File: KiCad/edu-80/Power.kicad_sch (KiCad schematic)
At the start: 5 parts, among them U11 CD4093, U12 4027, U13 4001, U16 7400

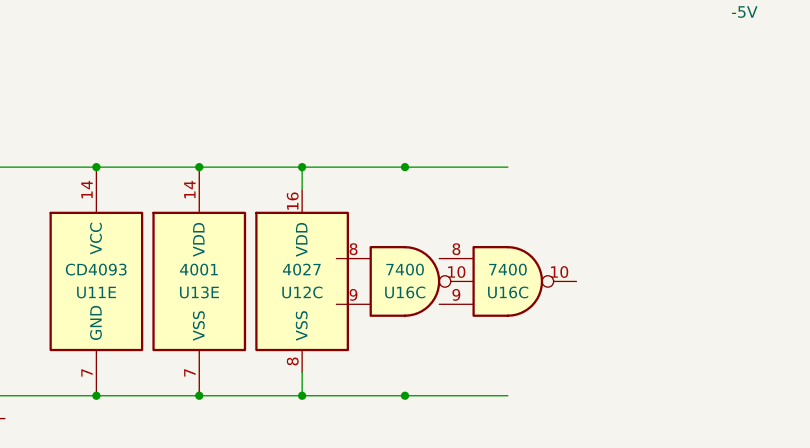
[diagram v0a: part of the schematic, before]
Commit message: Fixed lst of the errors, still two warnings
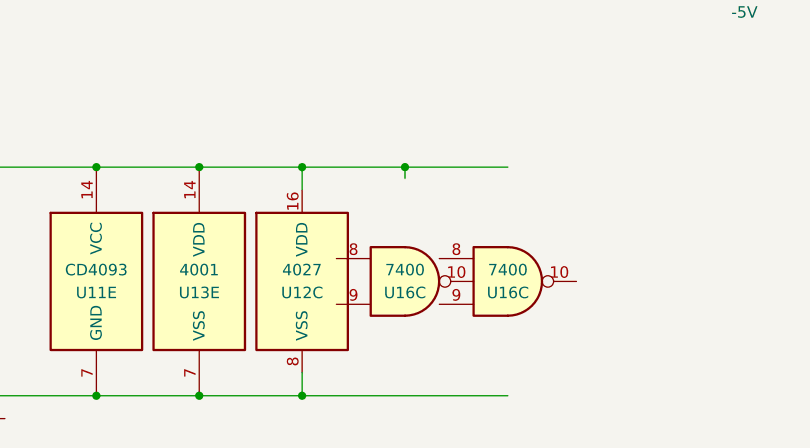
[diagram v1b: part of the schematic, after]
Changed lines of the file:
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@@
 (kicad_sch (version 20230121) (generator eeschema)
   (paper "A")
-  (junction (at 76.2 92.71) (diameter 0) (color 0 0 0 0)
-  )
   (junction (at 41.91 92.71) (diameter 0) (color 0 0 0 0)
   )
@@
   )
   (junction (at 53.34 92.71) (diameter 0) (color 0 0 0 0)
-  )
-  (junction (at 76.2 118.11) (diameter 0) (color 0 0 0 0)
   )
   (junction (at 114.3 68.58) (diameter 0) (color 0 0 0 0)
@@
   )
   (junction (at 88.9 52.07) (diameter 0) (color 0 0 0 0)
+  )
+  (junction (at 76.2 92.71) (diameter 0) (color 0 0 0 0)
   )
   (junction (at 139.7 68.58) (diameter 0) (color 0 0 0 0)
@@
     (stroke (width 0) (type default))
   )
-  (wire (pts (xy 76.2 92.71) (xy 87.63 92.71))
-    (stroke (width 0) (type default))
-  )
   (wire (pts (xy 64.77 92.71) (xy 76.2 92.71))
     (stroke (width 0) (type default))
@@
     (stroke (width 0) (type default))
   )
+  (wire (pts (xy 64.77 118.11) (xy 87.63 118.11))
+    (stroke (width 0) (type default))
+  )
   (wire (pts (xy 139.7 68.58) (xy 139.7 63.5))
     (stroke (width 0) (type default))
@@
     (stroke (width 0) (type default))
   )
-  (wire (pts (xy 63.5 31.75) (xy 63.5 38.1))
+  (wire (pts (xy 114.3 71.12) (xy 114.3 68.58))
     (stroke (width 0) (type default))
   )
-  (wire (pts (xy 64.77 118.11) (xy 76.2 118.11))
-    (stroke (width 0) (type default))
-  )
-  (wire (pts (xy 114.3 71.12) (xy 114.3 68.58))
+  (wire (pts (xy 63.5 31.75) (xy 63.5 38.1))
     (stroke (width 0) (type default))
   )
@@
     (stroke (width 0) (type default))
   )
-  (wire (pts (xy 76.2 118.11) (xy 87.63 118.11))
+  (wire (pts (xy 76.2 92.71) (xy 76.2 93.98))
     (stroke (width 0) (type default))
   )
@@
     (stroke (width 0) (type default))
   )
+  (wire (pts (xy 76.2 92.71) (xy 87.63 92.71))
+    (stroke (width 0) (type default))
+  )

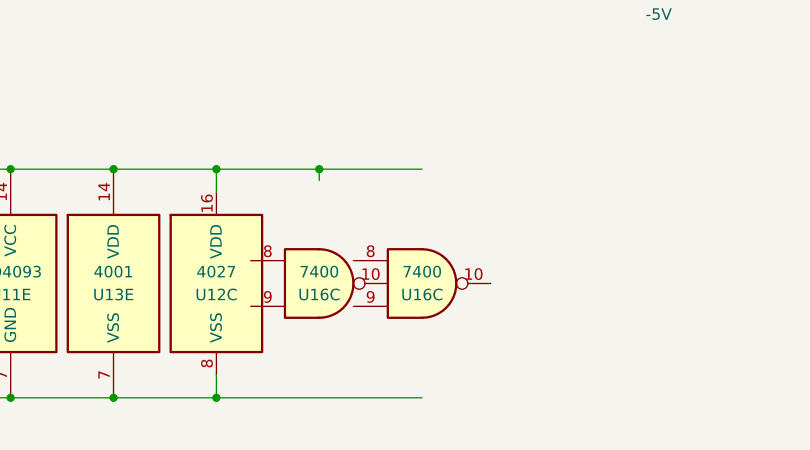
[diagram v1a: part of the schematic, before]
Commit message: Working on removing edu-80-rescue symbol library
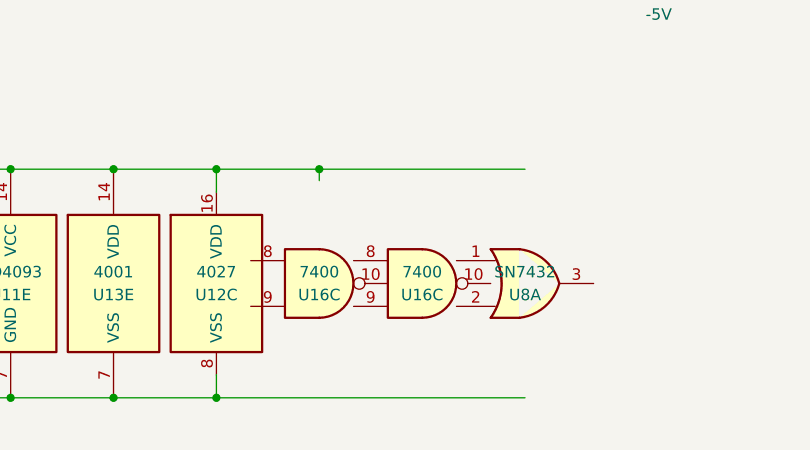
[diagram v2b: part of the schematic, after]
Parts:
- added U8: SN7432, symbol Edu-80_Symbols:SN7432
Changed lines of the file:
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@@
 (kicad_sch (version 20230121) (generator eeschema)
   (paper "A")
+  (junction (at 64.77 118.11) (diameter 0) (color 0 0 0 0)
+  )
   (junction (at 41.91 92.71) (diameter 0) (color 0 0 0 0)
   )
   (junction (at 38.1 34.29) (diameter 0) (color 0 0 0 0)
   )
-  (junction (at 64.77 118.11) (diameter 0) (color 0 0 0 0)
-  )
   (junction (at 53.34 92.71) (diameter 0) (color 0 0 0 0)
   )
@@
     (stroke (width 0) (type default))
   )
+  (wire (pts (xy 76.2 92.71) (xy 99.06 92.71))
+    (stroke (width 0) (type default))
+  )
   (wire (pts (xy 38.1 31.75) (xy 38.1 34.29))
     (stroke (width 0) (type default))
@@
     (stroke (width 0) (type default))
   )
-  (wire (pts (xy 64.77 118.11) (xy 87.63 118.11))
-    (stroke (width 0) (type default))
-  )
   (wire (pts (xy 139.7 68.58) (xy 139.7 63.5))
     (stroke (width 0) (type default))
@@
     (stroke (width 0) (type default))
   )
-  (wire (pts (xy 76.2 92.71) (xy 87.63 92.71))
+  (wire (pts (xy 64.77 118.11) (xy 99.06 118.11))
     (stroke (width 0) (type default))
   )
@@
         )
       )
+    )
+  )
+  (symbol (lib_id "Edu-80_Symbols:SN7432") (at 99.06 105.41 0) (unit 1)
+    (in_bom yes) (on_board yes) (dnp no)
+    (property "Reference" "U8" (at 99.06 106.68 0)
+      (effects (font (size 1.27 1.27)))
+    )
+    (property "Value" "SN7432" (at 99.06 104.14 0)
+      (effects (font (size 1.27 1.27)))
+    )
+    (property "Footprint" "" (at 99.06 105.41 0)
+      (effects (font (size 1.27 1.27)) hide)
+    )
+    (property "Datasheet" "" (at 99.06 105.41 0)
+      (effects (font (size 1.27 1.27)) hide)
+    )
+    (pin "1")
+    (pin "2")
+    (pin "3")
+    (pin "4")
+    (pin "5")
+    (pin "6")
+    (pin "10")
+    (pin "8")
+    (pin "9")
+    (pin "11")
+    (pin "12")
+    (pin "13")
+    (pin "14")
+    (pin "7")
+    (instances
+      (project "edu-80"
+        (path "/d19d6db6-a96a-43e3-aa50-c057821f7e22/00000000-0000-0000-0000-000063e35f90"
+          (reference "U8") (unit 1)
+        )
+        (path "/d19d6db6-a96a-43e3-aa50-c057821f7e22/00000000-0000-0000-0000-0000644ab222"
+          (reference "U8") (unit 5)
+        )
+      )

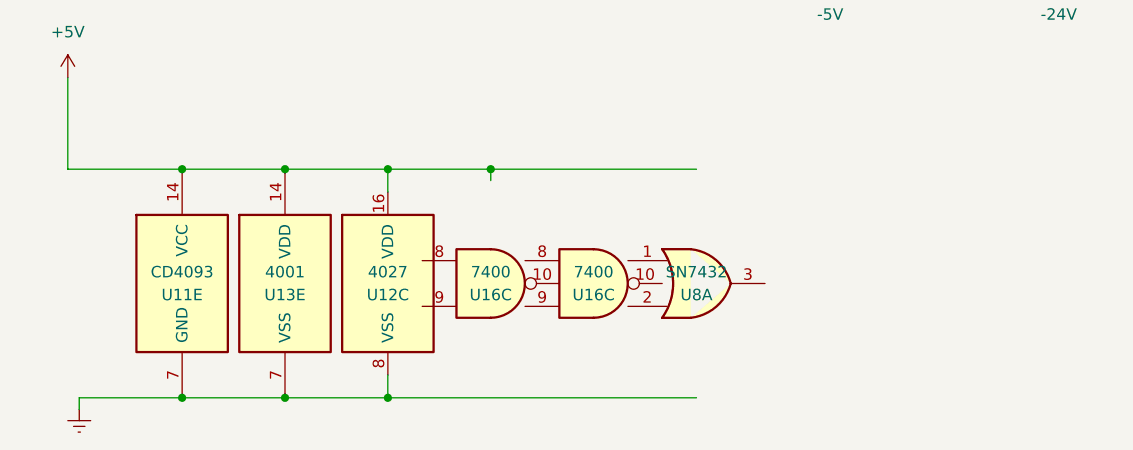
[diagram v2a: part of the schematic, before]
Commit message: Cleaning up the PAL-003 decoding, adding Modifications page.
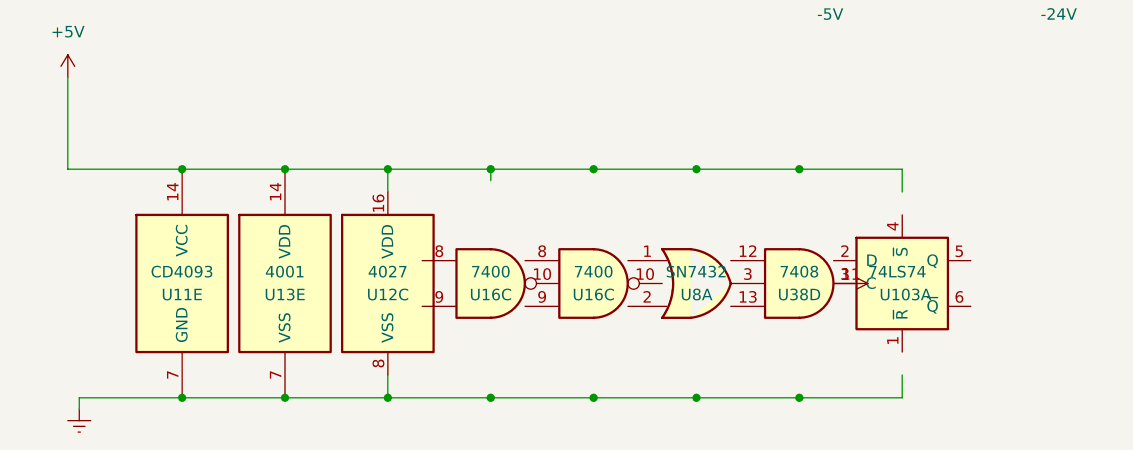
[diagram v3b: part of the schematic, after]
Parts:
- added U103: 74LS74, symbol 74xx:74LS74
- added U38: 7408, symbol Edu-80_Symbols:7408
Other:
- company: (none) -> Strangers
- title: (none) -> Edu-80 Z80 Trainer
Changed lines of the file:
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@@
 (kicad_sch (version 20230121) (generator eeschema)
   (paper "A")
+  (title_block
+    (title "Edu-80 Z80 Trainer")
+    (date "2023-06-03")
+    (rev "0.1")
+    (company "Strangers")
+    (comment 1 "Author: James D. Tucker")
+  )
+  (junction (at 38.1 34.29) (diameter 0) (color 0 0 0 0)
+  )
+  (junction (at 53.34 118.11) (diameter 0) (color 0 0 0 0)
+  )
+  (junction (at 87.63 118.11) (diameter 0) (color 0 0 0 0)
+  )
+  (junction (at 41.91 92.71) (diameter 0) (color 0 0 0 0)
+  )
+  (junction (at 114.3 68.58) (diameter 0) (color 0 0 0 0)
+  )
+  (junction (at 76.2 92.71) (diameter 0) (color 0 0 0 0)
+  )
+  (junction (at 53.34 92.71) (diameter 0) (color 0 0 0 0)
+  )
+  (junction (at 99.06 118.11) (diameter 0) (color 0 0 0 0)
+  )
+  (junction (at 64.77 92.71) (diameter 0) (color 0 0 0 0)
+  )
+  (junction (at 87.63 92.71) (diameter 0) (color 0 0 0 0)
+  )
+  (junction (at 110.49 92.71) (diameter 0) (color 0 0 0 0)
+  )
+  (junction (at 41.91 118.11) (diameter 0) (color 0 0 0 0)
+  )
+  (junction (at 110.49 118.11) (diameter 0) (color 0 0 0 0)
+  )
+  (junction (at 88.9 52.07) (diameter 0) (color 0 0 0 0)
+  )
+  (junction (at 139.7 68.58) (diameter 0) (color 0 0 0 0)
+  )
+  (junction (at 76.2 118.11) (diameter 0) (color 0 0 0 0)
+  )
+  (junction (at 99.06 92.71) (diameter 0) (color 0 0 0 0)
+  )
   (junction (at 64.77 118.11) (diameter 0) (color 0 0 0 0)
   )
-  (junction (at 41.91 92.71) (diameter 0) (color 0 0 0 0)
-  )
-  (junction (at 38.1 34.29) (diameter 0) (color 0 0 0 0)
-  )
-  (junction (at 53.34 92.71) (diameter 0) (color 0 0 0 0)
-  )
-  (junction (at 114.3 68.58) (diameter 0) (color 0 0 0 0)
-  )
-  (junction (at 64.77 92.71) (diameter 0) (color 0 0 0 0)
-  )
-  (junction (at 41.91 118.11) (diameter 0) (color 0 0 0 0)
-  )
-  (junction (at 53.34 118.11) (diameter 0) (color 0 0 0 0)
-  )
-  (junction (at 88.9 52.07) (diameter 0) (color 0 0 0 0)
-  )
-  (junction (at 76.2 92.71) (diameter 0) (color 0 0 0 0)
-  )
-  (junction (at 139.7 68.58) (diameter 0) (color 0 0 0 0)
+  (wire (pts (xy 99.06 118.11) (xy 110.49 118.11))
+    (stroke (width 0) (type default))
+  )
+  (wire (pts (xy 121.92 92.71) (xy 110.49 92.71))
+    (stroke (width 0) (type default))
+  )
+  (wire (pts (xy 41.91 92.71) (xy 53.34 92.71))
+    (stroke (width 0) (type default))
   )
   (wire (pts (xy 64.77 115.57) (xy 64.77 118.11))
     (stroke (width 0) (type default))
   )
-  (wire (pts (xy 41.91 92.71) (xy 53.34 92.71))
+  (wire (pts (xy 30.48 118.11) (xy 41.91 118.11))
+    (stroke (width 0) (type default))
+  )
+  (wire (pts (xy 41.91 118.11) (xy 53.34 118.11))
     (stroke (width 0) (type default))
   )
@@
     (stroke (width 0) (type default))
   )
+  (wire (pts (xy 87.63 92.71) (xy 99.06 92.71))
+    (stroke (width 0) (type default))
+  )
   (wire (pts (xy 139.7 71.12) (xy 139.7 68.58))
     (stroke (width 0) (type default))
   )
+  (wire (pts (xy 64.77 118.11) (xy 76.2 118.11))
+    (stroke (width 0) (type default))
+  )
+  (wire (pts (xy 29.21 92.71) (xy 41.91 92.71))
+    (stroke (width 0) (type default))
+  )
+  (wire (pts (xy 38.1 31.75) (xy 38.1 34.29))
+    (stroke (width 0) (type default))
+  )
+  (wire (pts (xy 194.31 39.37) (xy 194.31 46.99))
+    (stroke (width 0) (type default))
+  )
+  (wire (pts (xy 139.7 68.58) (xy 139.7 63.5))
+    (stroke (width 0) (type default))
+  )
+  (wire (pts (xy 121.92 115.57) (xy 121.92 118.11))
+    (stroke (width 0) (type default))
+  )
+  (wire (pts (xy 76.2 92.71) (xy 87.63 92.71))
+    (stroke (width 0) (type default))
+  )
+  (wire (pts (xy 99.06 92.71) (xy 110.49 92.71))
+    (stroke (width 0) (type default))
+  )
+  (wire (pts (xy 114.3 71.12) (xy 114.3 68.58))
+    (stroke (width 0) (type default))
+  )
+  (wire (pts (xy 63.5 31.75) (xy 63.5 38.1))
+    (stroke (width 0) (type default))
+  )
+  (wire (pts (xy 29.21 92.71) (xy 29.21 82.55))
+    (stroke (width 0) (type default))
+  )
+  (wire (pts (xy 88.9 52.07) (xy 88.9 46.99))
+    (stroke (width 0) (type default))
+  )
+  (wire (pts (xy 76.2 92.71) (xy 76.2 93.98))
+    (stroke (width 0) (type default))
+  )
+  (wire (pts (xy 121.92 95.25) (xy 121.92 92.71))
+    (stroke (width 0) (type default))
+  )
+  (wire (pts (xy 53.34 118.11) (xy 64.77 118.11))
+    (stroke (width 0) (type default))
+  )
+  (wire (pts (xy 53.34 92.71) (xy 64.77 92.71))
+    (stroke (width 0) (type default))
+  )
+  (wire (pts (xy 168.91 39.37) (xy 168.91 46.99))
+    (stroke (width 0) (type default))
+  )
+  (wire (pts (xy 64.77 92.71) (xy 64.77 95.25))
+    (stroke (width 0) (type default))
+  )
+  (wire (pts (xy 121.92 118.11) (xy 110.49 118.11))
+    (stroke (width 0) (type default))
+  )
+  (wire (pts (xy 114.3 68.58) (xy 114.3 63.5))
+    (stroke (width 0) (type default))
+  )
+  (wire (pts (xy 87.63 118.11) (xy 99.06 118.11))
+    (stroke (width 0) (type default))
+  )
   (wire (pts (xy 64.77 92.71) (xy 76.2 92.71))
     (stroke (width 0) (type default))
   )
-  (wire (pts (xy 41.91 118.11) (xy 53.34 118.11))
-    (stroke (width 0) (type default))
-  )
-  (wire (pts (xy 76.2 92.71) (xy 99.06 92.71))
-    (stroke (width 0) (type default))
-  )
-  (wire (pts (xy 38.1 31.75) (xy 38.1 34.29))
-    (stroke (width 0) (type default))
-  )
-  (wire (pts (xy 194.31 39.37) (xy 194.31 46.99))
-    (stroke (width 0) (type default))
-  )
-  (wire (pts (xy 139.7 68.58) (xy 139.7 63.5))
-    (stroke (width 0) (type default))
-  )
-  (wire (pts (xy 64.77 118.11) (xy 53.34 118.11))
-    (stroke (width 0) (type default))
-  )
-  (wire (pts (xy 114.3 71.12) (xy 114.3 68.58))
-    (stroke (width 0) (type default))
-  )
-  (wire (pts (xy 63.5 31.75) (xy 63.5 38.1))
-    (stroke (width 0) (type default))
-  )
-  (wire (pts (xy 41.91 118.11) (xy 30.48 118.11))
-    (stroke (width 0) (type default))
-  )
-  (wire (pts (xy 29.21 92.71) (xy 41.91 92.71))
-    (stroke (width 0) (type default))
-  )
-  (wire (pts (xy 29.21 92.71) (xy 29.21 82.55))
-    (stroke (width 0) (type default))
-  )
-  (wire (pts (xy 88.9 52.07) (xy 88.9 46.99))
-    (stroke (width 0) (type default))
-  )
-  (wire (pts (xy 76.2 92.71) (xy 76.2 93.98))
-    (stroke (width 0) (type default))
-  )
-  (wire (pts (xy 168.91 39.37) (xy 168.91 46.99))
-    (stroke (width 0) (type default))
-  )
-  (wire (pts (xy 64.77 118.11) (xy 99.06 118.11))
-    (stroke (width 0) (type default))
-  )
-  (wire (pts (xy 53.34 92.71) (xy 64.77 92.71))
-    (stroke (width 0) (type default))
-  )
-  (wire (pts (xy 64.77 92.71) (xy 64.77 95.25))
-    (stroke (width 0) (type default))
-  )
-  (wire (pts (xy 114.3 68.58) (xy 114.3 63.5))
+  (wire (pts (xy 76.2 118.11) (xy 87.63 118.11))
     (stroke (width 0) (type default))
   )
@@
     )
   )
+  (symbol (lib_id "74xx:74LS74") (at 121.92 105.41 0) (unit 1)
+    (in_bom yes) (on_board yes) (dnp no)
+    (property "Reference" "U103" (at 119.38 106.68 0)
+      (effects (font (size 1.27 1.27)) (justify left))
+    )
+    (property "Value" "74LS74" (at 118.11 104.14 0)
+      (effects (font (size 1.27 1.27)) (justify left))
+    )
+    (property "Footprint" "" (at 121.92 105.41 0)
+      (effects (font (size 1.27 1.27)) hide)
+    )
+    (property "Datasheet" "74xx/74hc_hct74.pdf" (at 121.92 105.41 0)
+      (effects (font (size 1.27 1.27)) hide)
+    )
+    (pin "1")
+    (pin "2")
+    (pin "3")
+    (pin "4")
+    (pin "5")
+    (pin "6")
+    (pin "10")
+    (pin "11")
+    (pin "12")
+    (pin "13")
+    (pin "8")
+    (pin "9")
+    (pin "14")
+    (pin "7")
+    (instances
+      (project "edu-80"
+        (path "/d19d6db6-a96a-43e3-aa50-c057821f7e22/400fb073-5ef0-450a-b07f-a4b615331875"
+          (reference "U103") (unit 1)
+        )
+        (path "/d19d6db6-a96a-43e3-aa50-c057821f7e22/00000000-0000-0000-0000-0000644ab222"
+          (reference "U103") (unit 3)
+        )
+      )
+    )
+  )
   (symbol (lib_id "power:Earth") (at 30.48 119.38 0) (unit 1)
     (in_bom yes) (on_board yes) (dnp no) (fields_autoplaced)
@@
         )
       )
+    )
+  )
+  (symbol (lib_id "Edu-80_Symbols:7408") (at 110.49 105.41 0) (unit 4)
+    (in_bom yes) (on_board yes) (dnp no)
+    (property "Reference" "U38" (at 110.49 106.68 0)
+      (effects (font (size 1.27 1.27)))
+    )
+    (property "Value" "7408" (at 110.49 104.14 0)
+      (effects (font (size 1.27 1.27)))
+    )
+    (property "Footprint" "" (at 110.49 105.41 0)
+      (effects (font (size 1.27 1.27)) hide)
+    )
+    (property "Datasheet" "http://www.ti.com/lit/gpn/sn7408" (at 110.49 111.76 0)
+      (effects (font (size 1.27 1.27)) hide)
+    )
+    (pin "1")
+    (pin "2")
+    (pin "3")
+    (pin "4")
+    (pin "5")
+    (pin "6")
+    (pin "10")
+    (pin "8")
+    (pin "9")
+    (pin "11")
+    (pin "12")
+    (pin "13")
+    (pin "14")
+    (pin "7")
+    (instances
+      (project "edu-80"
+        (path "/d19d6db6-a96a-43e3-aa50-c057821f7e22/400fb073-5ef0-450a-b07f-a4b615331875"
+          (reference "U38") (unit 4)
+        )
+        (path "/d19d6db6-a96a-43e3-aa50-c057821f7e22/00000000-0000-0000-0000-0000644ab222"
+          (reference "U101") (unit 5)
+        )
+      )

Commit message: Fixed ~IRQ vs. INT for PIO/CTC. Removed old (version 5) schematic files.
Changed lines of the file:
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@@
   (title_block
     (title "Edu-80 Z80 Trainer")
-    (date "2023-06-03")
+    (date "2023-06-05")
     (rev "0.1")
     (company "Strangers")
-    (comment 1 "Author: James D. Tucker")
+    (comment 4 "Author: James D. Tucker")
   )
   (junction (at 38.1 34.29) (diameter 0) (color 0 0 0 0)
   )
+  (junction (at 64.77 118.11) (diameter 0) (color 0 0 0 0)
+  )
   (junction (at 53.34 118.11) (diameter 0) (color 0 0 0 0)
   )
-  (junction (at 87.63 118.11) (diameter 0) (color 0 0 0 0)
+  (junction (at 87.63 92.71) (diameter 0) (color 0 0 0 0)
   )
   (junction (at 41.91 92.71) (diameter 0) (color 0 0 0 0)
@@
   (junction (at 53.34 92.71) (diameter 0) (color 0 0 0 0)
   )
-  (junction (at 99.06 118.11) (diameter 0) (color 0 0 0 0)
-  )
   (junction (at 64.77 92.71) (diameter 0) (color 0 0 0 0)
   )
-  (junction (at 87.63 92.71) (diameter 0) (color 0 0 0 0)
+  (junction (at 87.63 118.11) (diameter 0) (color 0 0 0 0)
+  )
+  (junction (at 110.49 118.11) (diameter 0) (color 0 0 0 0)
   )
   (junction (at 110.49 92.71) (diameter 0) (color 0 0 0 0)
   )
+  (junction (at 76.2 118.11) (diameter 0) (color 0 0 0 0)
+  )
   (junction (at 41.91 118.11) (diameter 0) (color 0 0 0 0)
   )
-  (junction (at 110.49 118.11) (diameter 0) (color 0 0 0 0)
+  (junction (at 99.06 118.11) (diameter 0) (color 0 0 0 0)
+  )
+  (junction (at 99.06 92.71) (diameter 0) (color 0 0 0 0)
   )
   (junction (at 88.9 52.07) (diameter 0) (color 0 0 0 0)
   )
   (junction (at 139.7 68.58) (diameter 0) (color 0 0 0 0)
-  )
-  (junction (at 76.2 118.11) (diameter 0) (color 0 0 0 0)
-  )
-  (junction (at 99.06 92.71) (diameter 0) (color 0 0 0 0)
-  )
-  (junction (at 64.77 118.11) (diameter 0) (color 0 0 0 0)
-  )
-  (wire (pts (xy 99.06 118.11) (xy 110.49 118.11))
-    (stroke (width 0) (type default))
-  )
-  (wire (pts (xy 121.92 92.71) (xy 110.49 92.71))
-    (stroke (width 0) (type default))
   )
   (wire (pts (xy 41.91 92.71) (xy 53.34 92.71))
@@
     (stroke (width 0) (type default))
   )
+  (wire (pts (xy 76.2 92.71) (xy 87.63 92.71))
+    (stroke (width 0) (type default))
+  )
   (wire (pts (xy 41.91 118.11) (xy 53.34 118.11))
     (stroke (width 0) (type default))
@@
     (stroke (width 0) (type default))
   )
+  (wire (pts (xy 139.7 71.12) (xy 139.7 68.58))
+    (stroke (width 0) (type default))
+  )
+  (wire (pts (xy 99.06 92.71) (xy 110.49 92.71))
+    (stroke (width 0) (type default))
+  )
   (wire (pts (xy 87.63 92.71) (xy 99.06 92.71))
     (stroke (width 0) (type default))
   )
-  (wire (pts (xy 139.7 71.12) (xy 139.7 68.58))
-    (stroke (width 0) (type default))
-  )
-  (wire (pts (xy 64.77 118.11) (xy 76.2 118.11))
+  (wire (pts (xy 110.49 92.71) (xy 121.92 92.71))
     (stroke (width 0) (type default))
   )
   (wire (pts (xy 29.21 92.71) (xy 41.91 92.71))
+    (stroke (width 0) (type default))
+  )
+  (wire (pts (xy 76.2 118.11) (xy 87.63 118.11))
     (stroke (width 0) (type default))
   )
@@
     (stroke (width 0) (type default))
   )
-  (wire (pts (xy 76.2 92.71) (xy 87.63 92.71))
-    (stroke (width 0) (type default))
-  )
-  (wire (pts (xy 99.06 92.71) (xy 110.49 92.71))
+  (wire (pts (xy 87.63 118.11) (xy 99.06 118.11))
     (stroke (width 0) (type default))
   )
@@
     (stroke (width 0) (type default))
   )
+  (wire (pts (xy 110.49 118.11) (xy 121.92 118.11))
+    (stroke (width 0) (type default))
+  )
   (wire (pts (xy 64.77 92.71) (xy 64.77 95.25))
     (stroke (width 0) (type default))
   )
-  (wire (pts (xy 121.92 118.11) (xy 110.49 118.11))
+  (wire (pts (xy 64.77 118.11) (xy 76.2 118.11))
     (stroke (width 0) (type default))
   )
@@
     (stroke (width 0) (type default))
   )
-  (wire (pts (xy 87.63 118.11) (xy 99.06 118.11))
-    (stroke (width 0) (type default))
-  )
   (wire (pts (xy 64.77 92.71) (xy 76.2 92.71))
     (stroke (width 0) (type default))
   )
-  (wire (pts (xy 76.2 118.11) (xy 87.63 118.11))
+  (wire (pts (xy 99.06 118.11) (xy 110.49 118.11))
     (stroke (width 0) (type default))
   )
